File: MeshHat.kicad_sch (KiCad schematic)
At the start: 5 parts, among them J1 RPi_GPIO, U3 CAT24C128

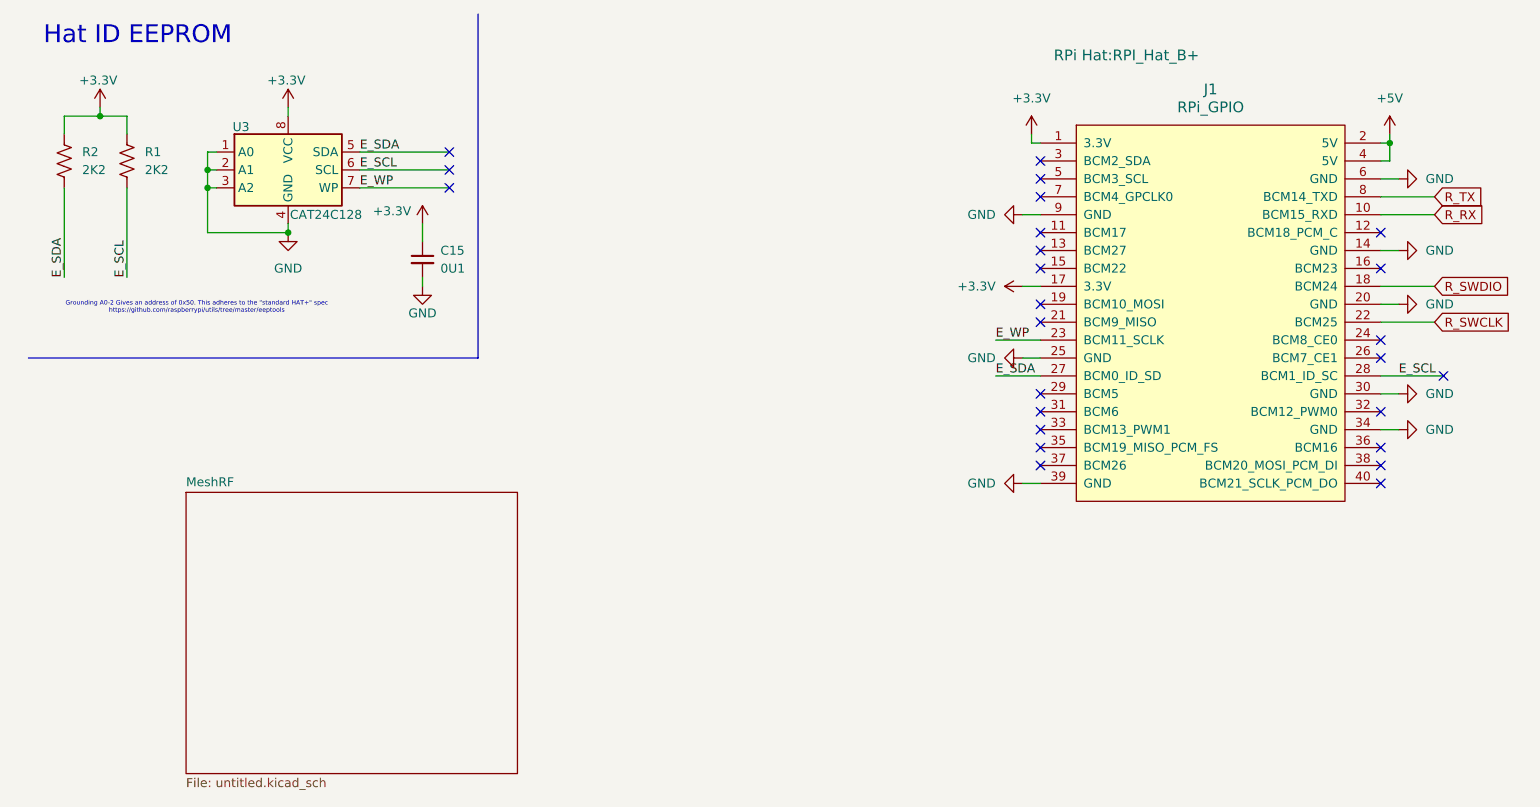
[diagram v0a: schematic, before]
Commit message: re-route the swdio lines
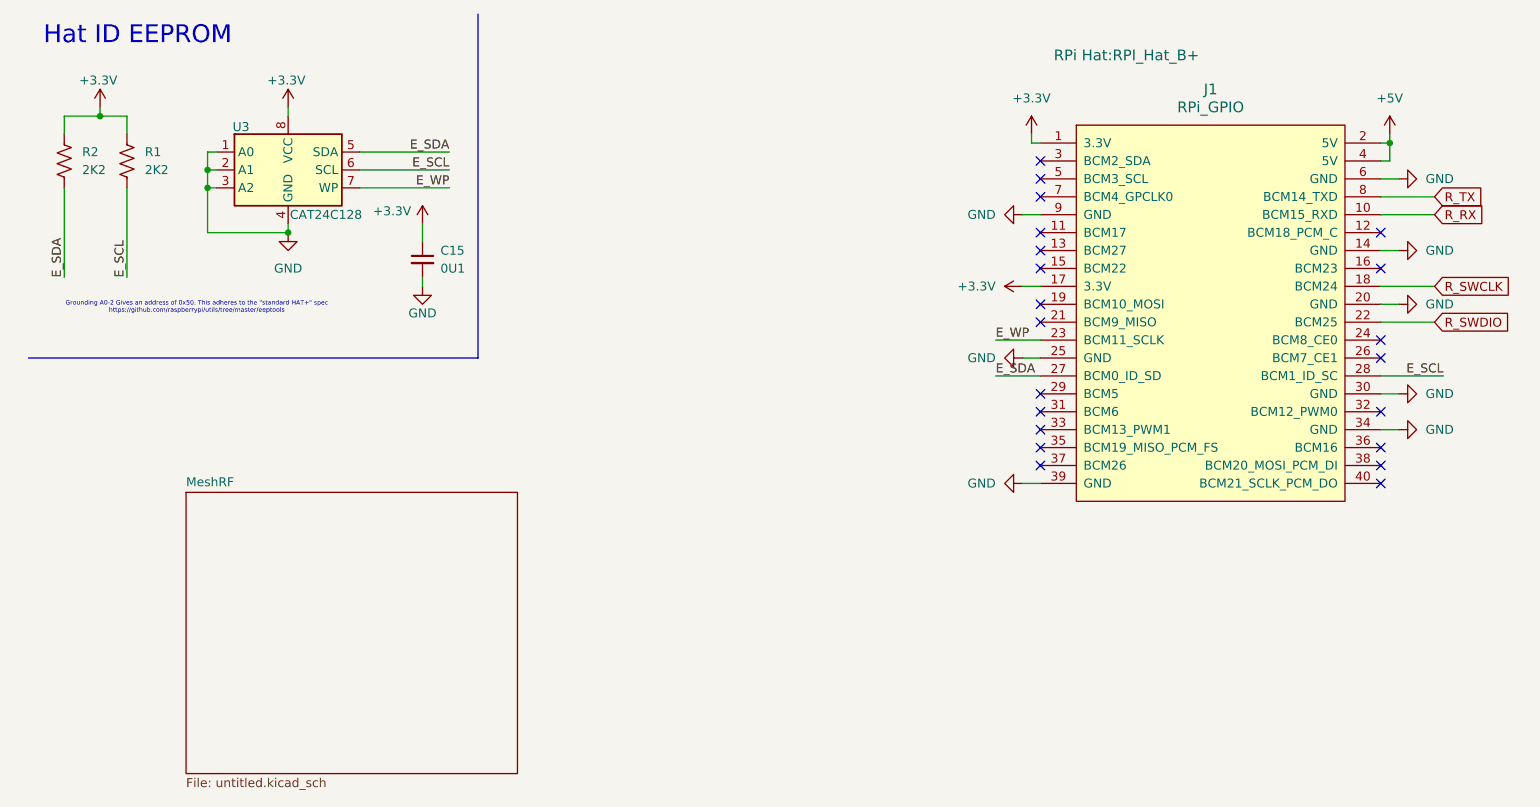
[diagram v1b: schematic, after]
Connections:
- net R_SWCLK: now also J1.18 (BCM24); no longer J1.22 (BCM25)
- net R_SWDIO: now also J1.22 (BCM25); no longer J1.18 (BCM24)
- no-connect marks 25 -> 21
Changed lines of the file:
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@@
-	)
-	(no_connect
-		(at 213.36 63.5)
 	)
 	(no_connect
@@
 	)
 	(no_connect
-		(at 72.39 34.29)
-	)
-	(no_connect
 		(at 204.47 73.66)
 	)
@@
 	)
 	(no_connect
-		(at 72.39 36.83)
-	)
-	(no_connect
 		(at 156.21 66.04)
 	)
-	(no_connect
-		(at 72.39 31.75)
-	)
 	(wire
 		(pts
@@
 	)
 	(label "E_SCL"
-		(at 207.01 63.5 0)
-		(effects
-			(font
-				(size 1.27 1.27)
-			)
-			(justify left bottom)
+		(at 213.36 63.5 180)
+		(effects
+			(font
+				(size 1.27 1.27)
+			)
+			(justify right bottom)
 		)
 	)
@@
 	)
 	(label "E_WP"
-		(at 59.69 36.83 0)
-		(effects
-			(font
-				(size 1.27 1.27)
-			)
-			(justify left bottom)
+		(at 72.39 36.83 180)
+		(effects
+			(font
+				(size 1.27 1.27)
+			)
+			(justify right bottom)
 		)
 	)
 	(label "E_SCL"
-		(at 59.69 34.29 0)
-		(effects
-			(font
-				(size 1.27 1.27)
-			)
-			(justify left bottom)
+		(at 72.39 34.29 180)
+		(effects
+			(font
+				(size 1.27 1.27)
+			)
+			(justify right bottom)
 		)
 	)
@@
 	)
 	(label "E_SDA"
-		(at 59.69 31.75 0)
-		(effects
-			(font
-				(size 1.27 1.27)
-			)
-			(justify left bottom)
+		(at 72.39 31.75 180)
+		(effects
+			(font
+				(size 1.27 1.27)
+			)
+			(justify right bottom)
 		)
 	)
@@
 	(global_label "R_SWDIO"
 		(shape input)
-		(at 212.09 50.8 0)
+		(at 212.09 55.88 0)
 		(fields_autoplaced yes)
 		(effects
@@
 		)
 		(property "Intersheetrefs" "${INTERSHEET_REFS}"
-			(at 223.179 50.8 0)
+			(at 223.179 55.88 0)
 			(hide yes)
 			(show_name no)
@@
 	(global_label "R_SWCLK"
 		(shape input)
-		(at 212.09 55.88 0)
+		(at 212.09 50.8 0)
 		(fields_autoplaced yes)
 		(effects
@@
 		)
 		(property "Intersheetrefs" "${INTERSHEET_REFS}"
-			(at 223.5418 55.88 0)
+			(at 223.5418 50.8 0)
 			(hide yes)
 			(show_name no)

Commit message: WIP
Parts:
- J1: footprint RPi Hat:RPI_Hat_B+ -> RPi_Hat:RPI_Hat_B+
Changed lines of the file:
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@@
 			)
 		)
-		(property "Footprint" "RPi Hat:RPI_Hat_B+"
+		(property "Footprint" "RPi_Hat:RPI_Hat_B+"
 			(at 168.402 18.034 0)
 			(show_name no)
